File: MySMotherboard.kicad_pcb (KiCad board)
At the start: 2 copper layers, 26.2 x 45.1 mm, 53 parts, among them SW1 RST, SW2 BTN, U1 MCP1640Cx-xCHY, U2 APE8865Y5-30-HF-3, U3 ATmega328PB-A, U4 AT25xxx, U5 RFM69HW, U6 ATSHA204A, U7 AP63205WU, U8 SP3481EN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

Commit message: change bypass capacitor for buck converter from 0603 to 0402
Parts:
- C11: value 22u -> 10u
- C6: footprint Capacitor_SMD:C_0603_1608Metric_Pad1.08x0.95mm_HandSolder -> Capacitor_SMD:C_0402_1005Metric_Pad0.74x0.62mm_HandSolder
- moved C6 3.83 mm to (153.7, 115.8), turned to 180 degrees
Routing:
- net Net-(U7-SW): track 9.14 -> 4.53 mm
- net Net-(U7-BST): track 4.31 -> 1.51 mm

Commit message: add pull-up resistor for RFM69W NSS pin
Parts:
- added R1: 1M, Resistor_SMD:R_0603_1608Metric, F.Cu at (154.1, 104.7)
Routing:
- net VCC: track 114.1 -> 116.7 mm
- net D10: track 41.6 -> 43.0 mm
- net D9: track 34.5 -> 35.2 mm
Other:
- board text added: "MySMotherboard v1.5"
- board text removed: "MySMotherboard v1.4"

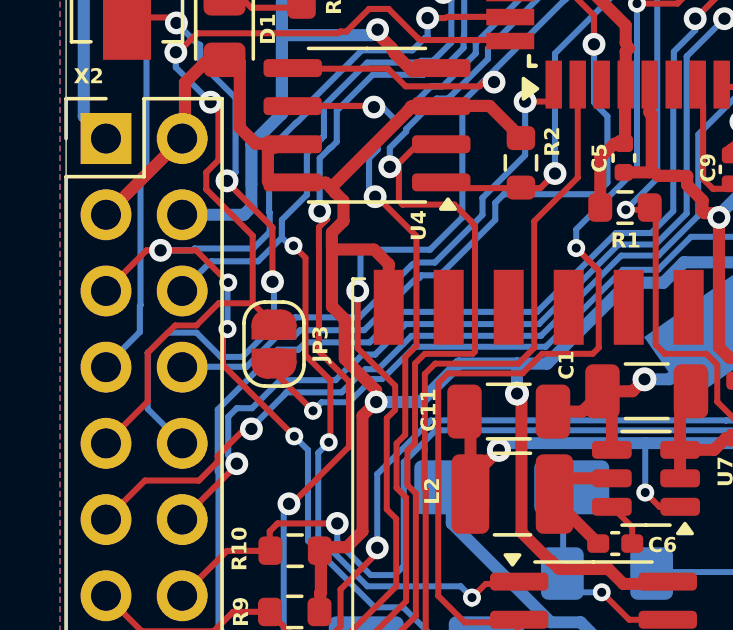
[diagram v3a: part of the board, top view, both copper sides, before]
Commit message: add option to connect RFM69W irq to pin 3
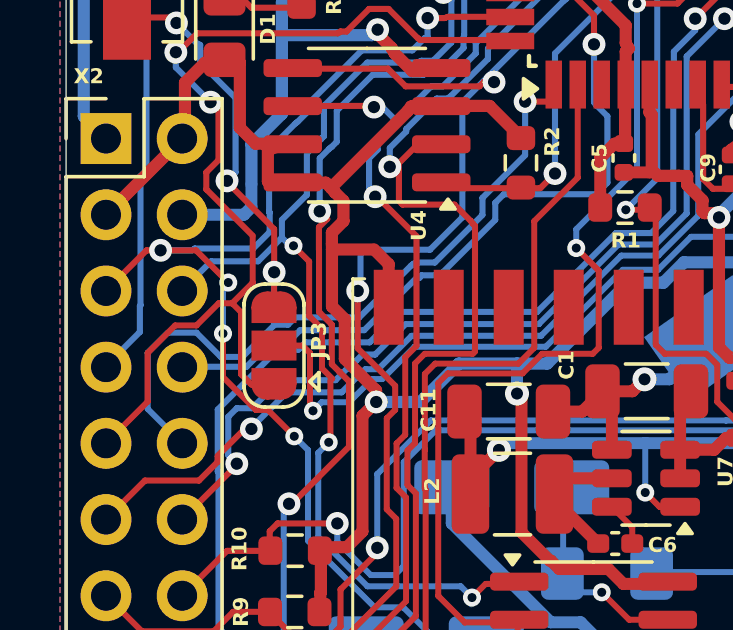
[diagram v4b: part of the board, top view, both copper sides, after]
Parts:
- JP3: footprint Jumper:SolderJumper-2_P1.3mm_Open_RoundedPad1.0x1.5mm -> Jumper:SolderJumper-3_P1.3mm_Open_RoundedPad1.0x1.5mm
- turned JP3 to 90 degrees
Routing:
- net D2: track 31.3 -> 33.3 mm
- net Net-(JP3-C): track 21.3 -> 22.5 mm
- net D3: track 36.7 -> 37.9 mm
